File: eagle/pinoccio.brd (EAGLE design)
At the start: 25.4 x 50.8 mm, 70 parts, among them IC1 ATMEGA16U2QFN32, J1 AVR_SPI_PRG_6, Q1 16MHz, Q2 32.768k, Q3 16MHz, Q4 MOSFET-PCHANNELSMD, U1 MCP73832, U2 TPS78233, U4 ATMEGA128RFA1, X1 USB-MICROB, Y2 ANTENNA2SMD5

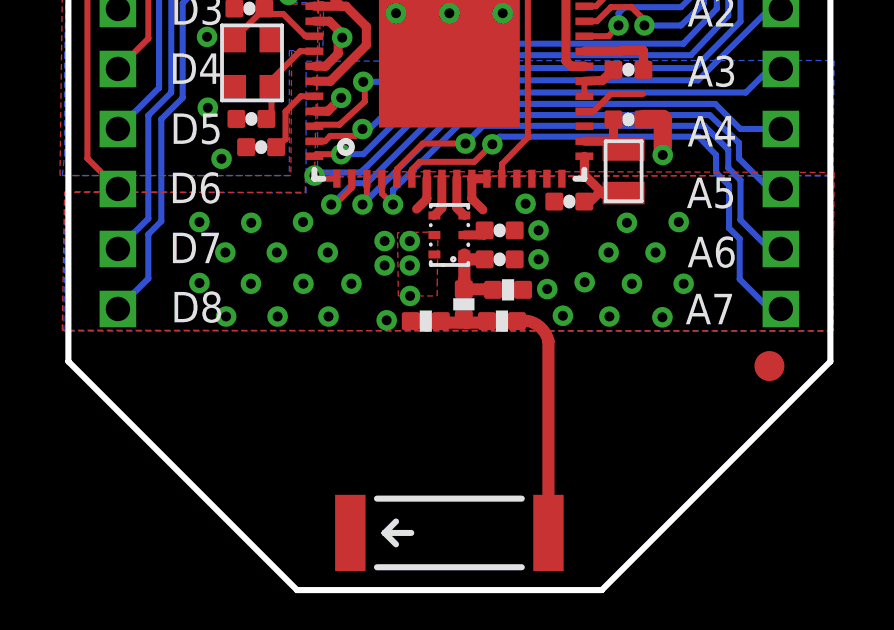
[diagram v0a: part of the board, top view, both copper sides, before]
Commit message: update pi network components
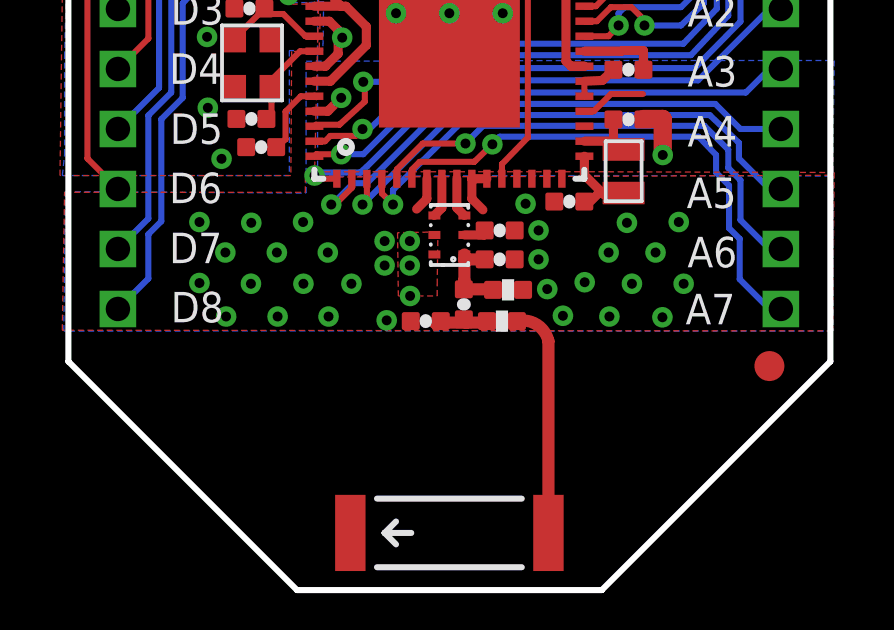
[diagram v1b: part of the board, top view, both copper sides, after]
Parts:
- removed R23: 1.0pF, Pinoccio:0402-RES
- added C23: 1.0pF, Pinoccio:0402-CAP
- L2: device Pinoccio:0402-RES -> Pinoccio:0402-CAP
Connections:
- net GND: now also C23.2; no longer R23.2
- net N$27: now also C23.1; no longer R23.1
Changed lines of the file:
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@@
 <element name="R20" library="Pinoccio" package="0402-RES" value="100k" x="14.732" y="45.2374" smashed="yes"/>
 <element name="R21" library="Pinoccio" package="0402-RES" value="DNI" x="14.6558" y="10.0076" smashed="yes"/>
-<element name="L2" library="Pinoccio" package="0402-RES" value="4.7nH" x="13.1826" y="9.525" smashed="yes" rot="R270"/>
-<element name="R23" library="Pinoccio" package="0402-RES" value="1.0pF" x="11.9126" y="8.9662" smashed="yes" rot="R180"/>
+<element name="L2" library="Pinoccio" package="0402-CAP" value="4.7nH" x="13.1826" y="9.525" smashed="yes" rot="R270"/>
+<element name="C23" library="Pinoccio" package="0402-CAP" value="1.0pF" x="11.9126" y="8.9662" smashed="yes" rot="R180"/>
 <element name="R24" library="Pinoccio" package="0402-RES" value="0" x="14.4526" y="8.9662" smashed="yes"/>
 <element name="Q4" library="Pinoccio" package="SOT23-3" value="MOSFET-PCHANNELSMD" x="18.4556" y="42.857" smashed="yes" rot="R270"/>
@@
 <via x="4.6482" y="16.0774" extent="1-16" drill="0.3302"/>
 <contactref element="R20" pad="2"/>
-<contactref element="R23" pad="2"/>
+<contactref element="C23" pad="2"/>
 <contactref element="R21" pad="2"/>
 <polygon width="0.2032" layer="16">
@@
 <contactref element="L2" pad="2"/>
 <contactref element="R24" pad="1"/>
-<contactref element="R23" pad="1"/>
-<contactref element="R23" pad="1"/>
+<contactref element="C23" pad="1"/>
+<contactref element="C23" pad="1"/>
 <wire x1="13.9526" y1="8.9662" x2="14.097" y2="8.9154" width="0.4064" layer="1"/>
 <wire x1="14.097" y1="8.9154" x2="14.1224" y2="8.9916" width="0.4064" layer="1"/>

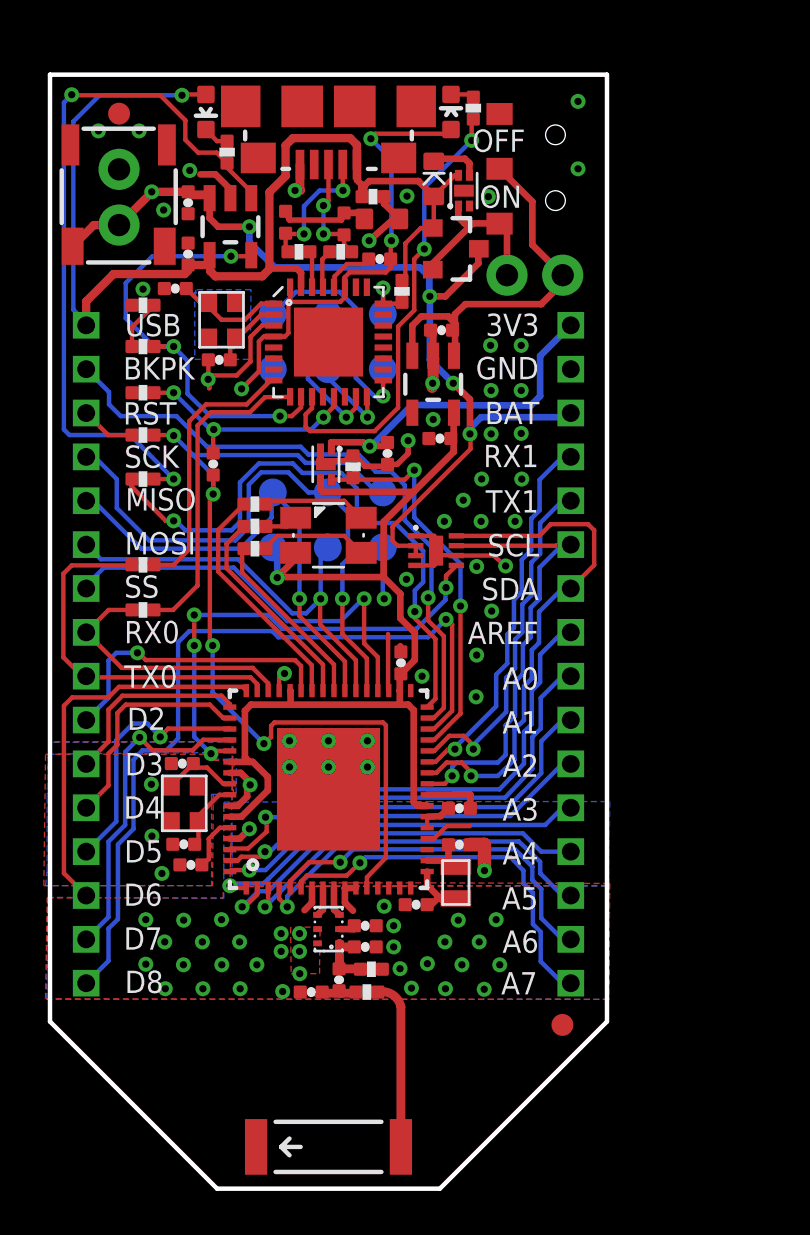
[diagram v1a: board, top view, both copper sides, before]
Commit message: updated names of components for assembly
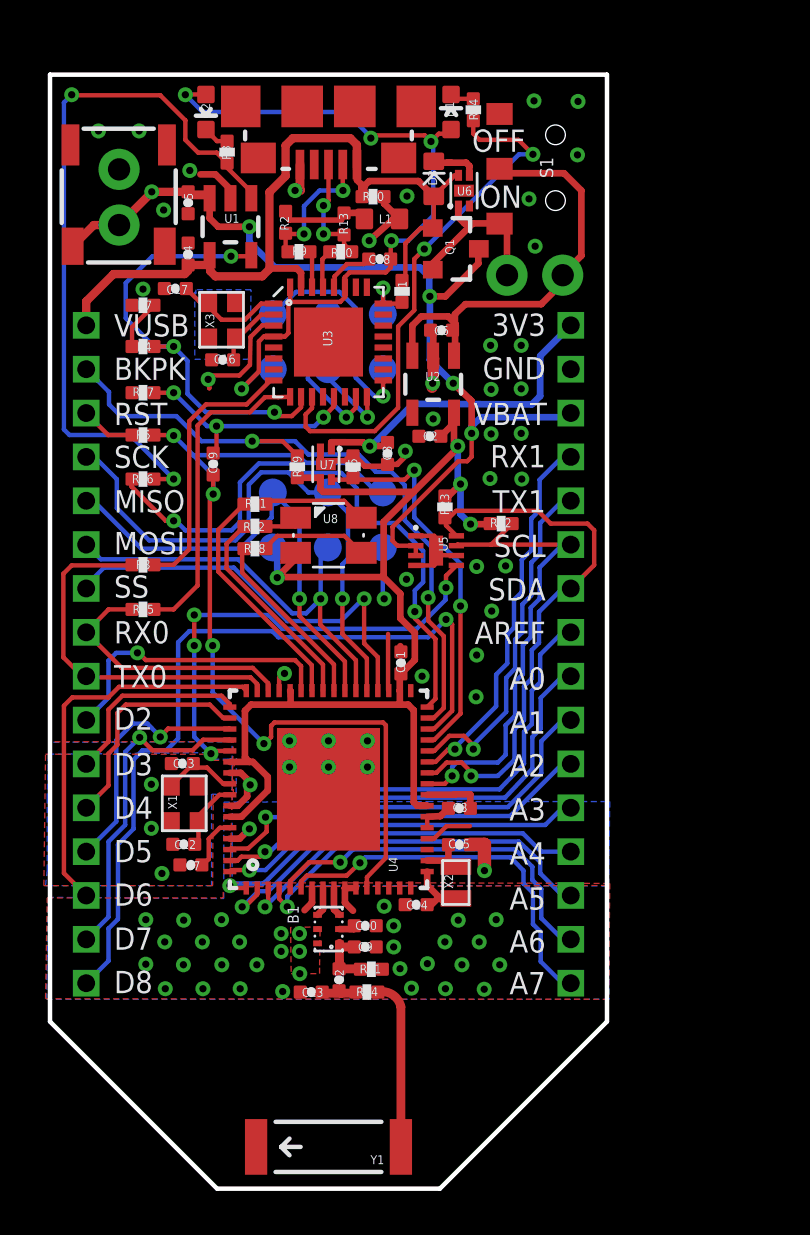
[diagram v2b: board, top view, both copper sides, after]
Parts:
- removed JP3, JP5: FIDUCIAL1X2, Pinoccio:FIDUCIAL-1X2
- removed Q2: 32.768k, BeanLabs:CRYSTAL-SMD-2X1.2-ABS06
- removed Q3: 16MHz, BeanLabs:CRYSTAL-SMD-2.5X2-ABM10
- removed Q4: MOSFET-PCHANNELSMD, Pinoccio:SOT23-3
- added R19, R22, R23: 2K, Pinoccio:0402-RES
- added USB-JACK: USB-MICROB, Pinoccio:USB-MICROB
- added X2: 32.768k, Pinoccio:CRYSTAL-SMD-2X1.2-ABS06
- added X3: 16MHz, Pinoccio:CRYSTAL-SMD-2.5X2-ABM10
- B1: value BALUN0805 -> BALUN
- C19, C3: value 100nF -> 0.1uF
- D3: value DIODE-SCHOTTKY -> (none)
- L1: value BML15H0603 -> BEAD
- Q1: value 16MHz -> PFET; device BeanLabs:CRYSTAL-SMD-2.5X2-ABM10 -> Pinoccio:SOT23-3
- R1, R16: value 2k -> 2K
- R13, R2: value VARISTOR0402 -> VAR
- R15, R17, R8: value 1k -> 1K
- U3: value ATMEGA16U2QFN32 -> ATMEGA16U2
- U4: value ATMEGA128RFA1 -> ATMEGA256RFR2
- U5: value MAX17048DFN8 -> MAX17048
- U6, U7: value SWITCH-MOSFETTDFN4 -> SWITCH
- U8: value LED-RGBPLCC4 -> LED-RGB
- X1: value USB-MICROB -> 16MHz; device Pinoccio:USB-MICROB -> Pinoccio:CRYSTAL-SMD-2.5X2-ABM10
- moved X1 32.5 mm to (6.12, 17.6), turned to 90 degrees
- moved Q1 28.1 mm to (18.5, 42.9), turned to 270 degrees
- moved C2 0.47 mm to (17.3, 34.3)
- moved C16 0.15 mm to (7.87, 37.8)
- moved R14 0.08 mm to (19.3, 49.2)
- renumbered IC1 to U3, JP1 to J3, JP2 to J4, JP4 to J2, S2 to S1, U$1 to U8, U$2 to U6, U$4 to U5, U$5 to U7, Y2 to Y1
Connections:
- net BKPK-BUS: now also R19.2
- net GND: now also USB-JACK.GND, X1.P$2, X1.P$4, X3.P$2, X3.P$4; no longer X1.GND
- net N$15: now also X1.P$1; no longer Q1.P$1
- net N$16: now also X1.P$3; no longer Q1.P$3
- net N$17: now also X2.P$1; no longer Q2.P$1
- net N$18: now also X2.P$2; no longer Q2.P$2
- net N$19: now also X3.P$1; no longer Q3.P$1
- net N$2: now also USB-JACK.D-; no longer X1.D-
- net N$21: now also X3.P$3; no longer Q3.P$3
- net N$43: now also USB-JACK.D+; no longer X1.D+
- net N$51: now also Q1.2; no longer Q4.2
- net SCL: now also R22.2
- net SDA: now also R23.2
- net UCAP: now also D2.A
- net VBAT: now also Q1.3; no longer Q4.3
- net VCC: now also R19.1, R22.1, R23.1
- net VUSB: now also Q1.1, USB-JACK.VBUS; no longer D2.A, Q4.1, X1.VBUS
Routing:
- net VUSB: track 53.4 -> 37.4 mm, vias 1 -> 0
- net UCAP: track 24.0 -> 35.2 mm, vias 3 -> 5
- net VCC: track 49.3 -> 57.4 mm, vias 1 -> 4
- net N$59: track 20.8 -> 24.4 mm
- net GND: track 50.1 -> 46.7 mm, vias 81 -> 79
- net BKPK-BUS: track 29.0 -> 31.4 mm, vias 1 -> 2
- net VIN: track 17.9 -> 20.2 mm
- net SDA: track 23.7 -> 25.3 mm
- net SCL: track 20.6 -> 22.0 mm
- net N$19: track 4.02 -> 3.39 mm
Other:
- board text added: "2013-08-15"
- board text added: "Pinoccio(tm) v1.0"
- board text added: "VBAT"
- board text added: "VUSB"
- board text added: "pinoccio v1.0"
- board text removed: "BAT"
- board text removed: "Pinoccio(tm) v0.13"
- board text removed: "USB"
- board text removed: "pinoccio v0.13"

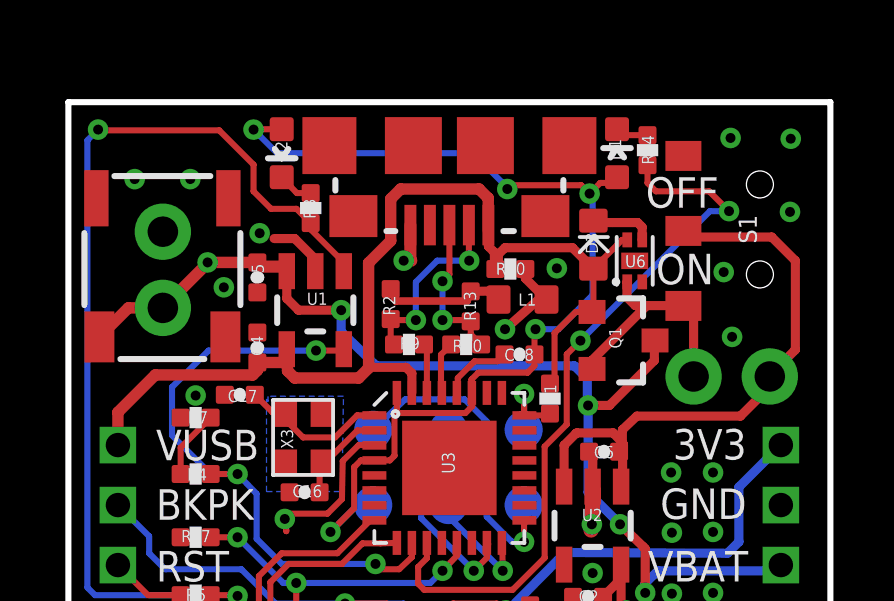
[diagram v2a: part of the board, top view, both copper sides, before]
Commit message: Add BOM and labels for jumpers
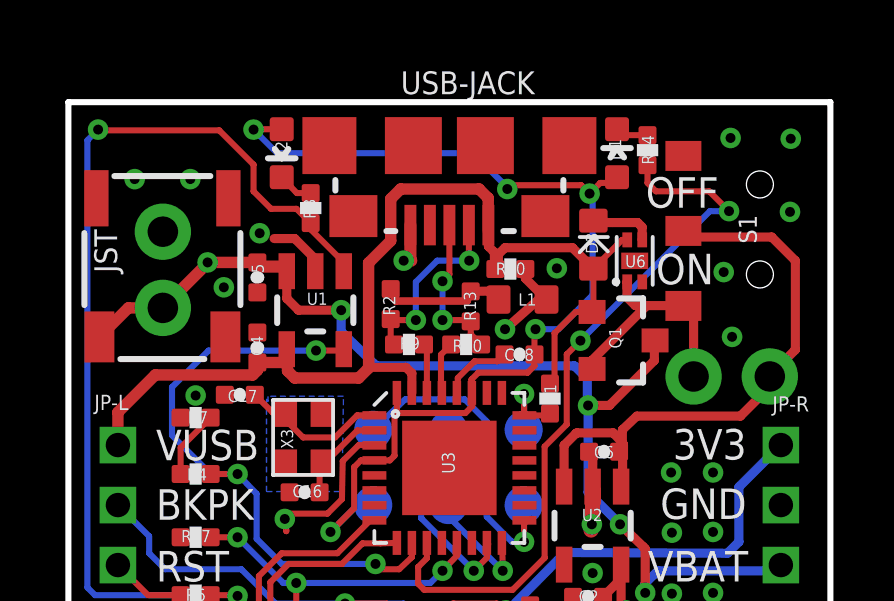
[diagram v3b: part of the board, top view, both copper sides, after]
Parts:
- C10: value 22pF -> DNI
- JST: value JST Bat -> (none)
- R19: value 2K -> 100K
- USB-JACK: value USB-MICROB -> (none)
- renumbered BATT to JST
